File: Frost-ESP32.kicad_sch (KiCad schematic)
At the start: 28 parts, among them J1 Micro_SD_Card, J2 CAN, J3 USB_C_Receptacle, J4 Conn_01x10, SW1 SW_Push, U1 ESP32-C3-WROOM-02, U2 AP2112K-3.3, U3 TJA1051T-3

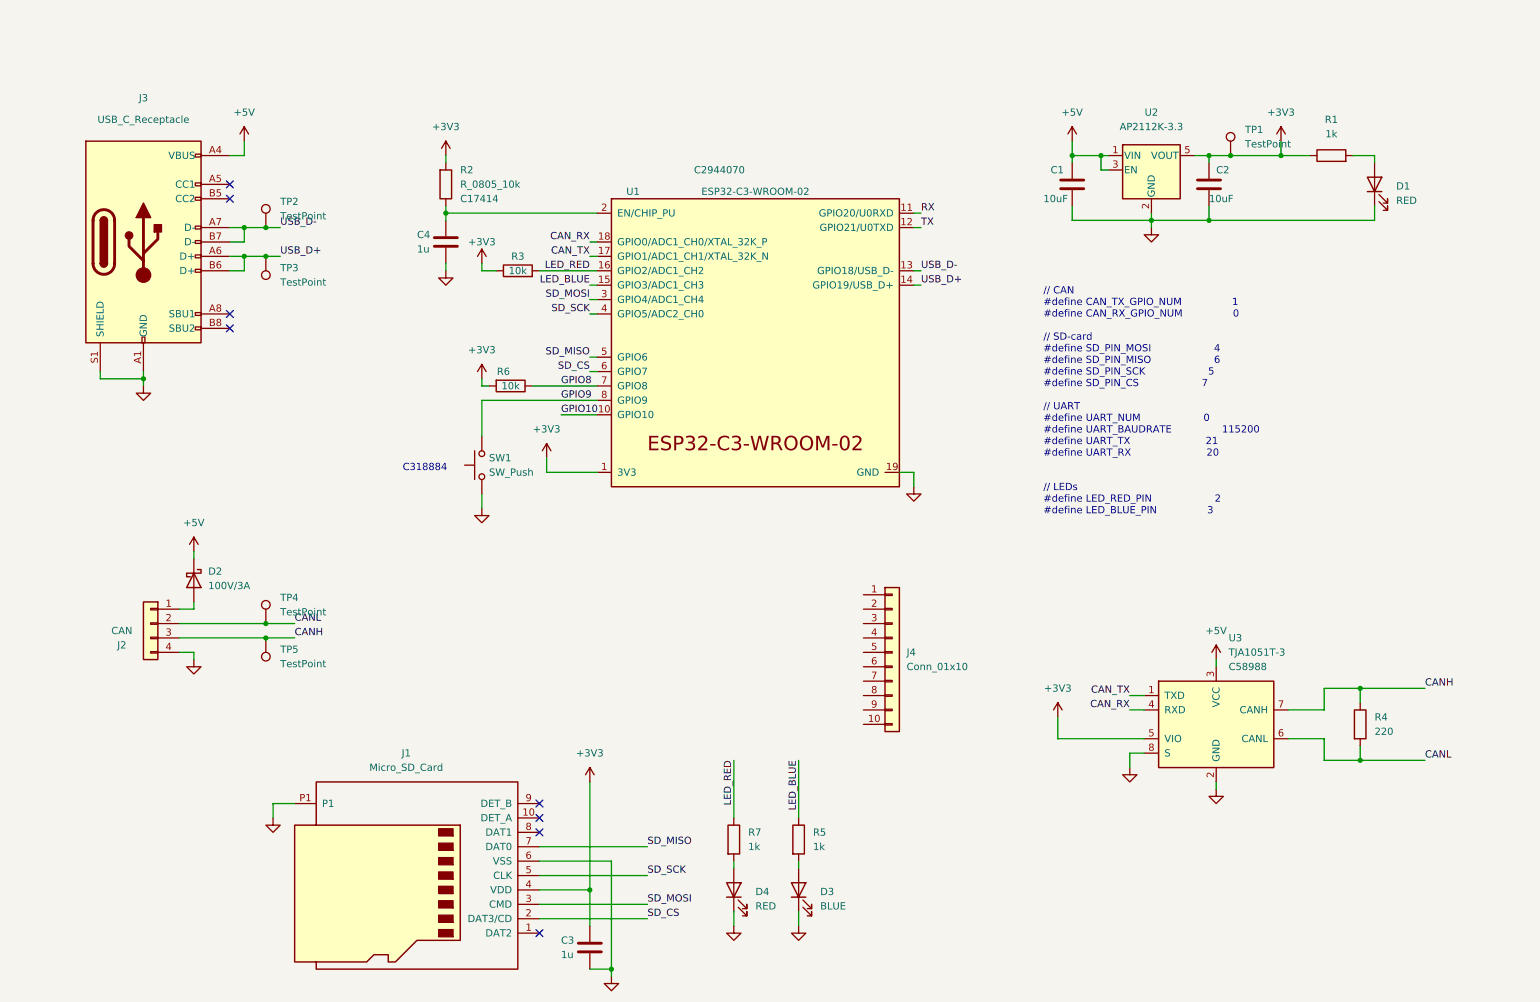
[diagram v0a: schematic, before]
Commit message: moved some symbols to fair library
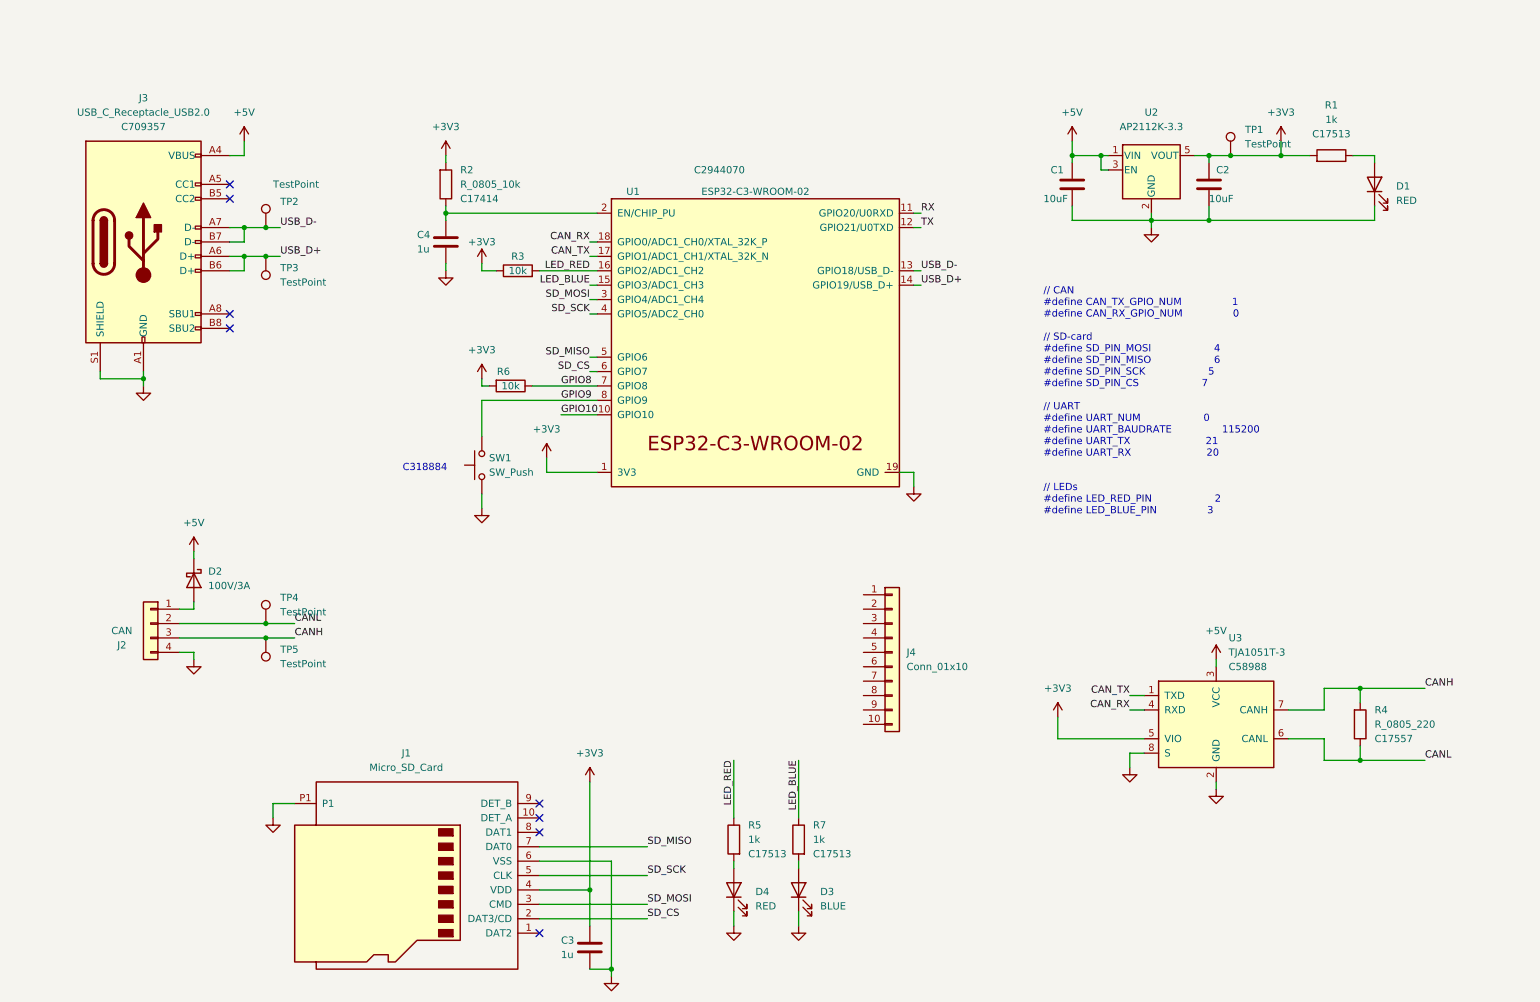
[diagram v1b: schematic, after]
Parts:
- removed J3: USB_C_Receptacle, Connector_USB:USB_C_Receptacle_XKB_U262-16XN-4BVC11, symbol Connector:USB_C_Receptacle_USB2.0
- removed R1, R5, R7: 1k, Resistor_SMD:R_0805_2012Metric, symbol Device:R
- removed R4: 220, Resistor_SMD:R_0805_2012Metric, symbol Device:R
- added J3: USB_C_Receptacle_USB2.0, Connector_USB:USB_C_Receptacle_XKB_U262-16XN-4BVC11, symbol Fair:USB_C_Receptacle_USB2.0
- added R1, R5, R7: 1k, Resistor_SMD:R_0805_2012Metric, symbol Fair:R_0805_1k
- added R4: R_0805_220, Resistor_SMD:R_0805_2012Metric, symbol Fair:R_0805_220
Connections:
- net +3V3: now also R1.1
- net +5V: now also J3.A4 (VBUS), J3.A9 (VBUS), J3.B4 (VBUS), J3.B9 (VBUS)
- net CANH: now also R4.1
- net CANL: now also R4.2
- net GND: now also J3.A1 (GND), J3.A12 (GND), J3.B1 (GND), J3.B12 (GND), J3.S1 (SHIELD)
- net LED_BLUE: now also R7.2
- net LED_RED: now also R5.2
- net USB_D+: now also J3.A6 (D+), J3.B6 (D+)
- net USB_D-: now also J3.A7 (D-), J3.B7 (D-)
- net at D1.2 (A): now also R1.2
- net at D3.2 (A): now also R7.1
- net at D4.2 (A): now also R5.1

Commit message: After ordering v0.1
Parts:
- removed C1, C2: 10uF, Capacitor_SMD:C_0805_2012Metric, symbol Device:C
- removed C3, C4: 1u, Capacitor_SMD:C_0805_2012Metric, symbol Device:C
- removed D1, D4: RED, LED_SMD:LED_0805_2012Metric, symbol Device:LED
- removed D3: BLUE, LED_SMD:LED_0603_1608Metric, symbol Device:LED
- removed J1: Micro_SD_Card, espressif:MOLEX_503398-1892, symbol Connector:Micro_SD_Card_Det
- removed J2: CAN, Connector_JST:JST_PH_B4B-PH-K_1x04_P2.00mm_Vertical, symbol Connector_Generic:Conn_01x04
- removed J3: USB_C_Receptacle_USB2.0, Connector_USB:USB_C_Receptacle_XKB_U262-16XN-4BVC11, symbol Fair:USB_C_Receptacle_USB2.0
- removed J4: Conn_01x10, Connector_PinHeader_2.54mm:PinHeader_1x10_P2.54mm_Vertical, symbol Connector_Generic:Conn_01x10
- removed R1, R5, R7: 1k, Resistor_SMD:R_0805_2012Metric, symbol Fair:R_0805_1k
- removed R2: R_0805_10k, Resistor_SMD:R_0805_2012Metric, symbol Fair:R_0805_10k
- removed R3, R6: 10k, Resistor_SMD:R_0805_2012Metric, symbol Device:R
- removed R4: R_0805_220, Resistor_SMD:R_0805_2012Metric, symbol Fair:R_0805_220
- removed SW1: SW_Push, Button_Switch_SMD:SW_Push_1P1T_XKB_TS-1187A, symbol Switch:SW_Push
- added C1, C2: 10uF/6.3V, Capacitor_SMD:C_0402_1005Metric, symbol Fair:C_0402_10uF/6.3V
- added C3: 1uF/25V, Capacitor_SMD:C_0402_1005Metric, symbol Fair:C_0402_1uF/25V
- added D1: Red, LED_SMD:LED_0603_1608Metric, symbol Fair:LED_0603_Red
- added D3: Blue, LED_SMD:LED_0603_1608Metric, symbol Fair:LED_BLUE_0603
- added D4: Emerald, LED_SMD:LED_0603_1608Metric, symbol Fair:LED_0603_Emerald
- added D5: 100V/3A, Diode_SMD:D_SOD-123F, symbol Device:D_Schottky
- added H1, H2: MountingHole, MountingHole:MountingHole_3.2mm_M3, symbol Mechanical:MountingHole
- added J1: Micro_SD_Card, Fair:MOLEX_503398-1892, symbol Fair:Micro_SD_Card_Det
- added J2: CAN, Connector_PinHeader_1.27mm:PinHeader_1x10_P1.27mm_Vertical, symbol Connector_Generic:Conn_01x10
- added J3: USB__B_Micro_Horizontal, Connector_USB:USB_Micro-B_Molex_47346-0001, symbol Fair:USB__B_Micro_Horizontal
- added R1, R5, R7: 1k, Resistor_SMD:R_0402_1005Metric, symbol Fair:R_0402_1k
- added R2, R3, R6: 10k, Resistor_SMD:R_0402_1005Metric, symbol Fair:R_0402_10k
- added R4: 220, Resistor_SMD:R_0402_1005Metric, symbol Fair:R_0402_220
- added S1: TL3340AF160QG, Fair:SW_TL3340AF160QG, symbol Fair:Switch_SMD_TL3340AF160QG
- added TP6, TP7: TestPoint, TestPoint:TestPoint_Pad_D1.0mm, symbol Connector:TestPoint
- U1: LCSC C2944070 -> C2934560
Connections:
- net +3V3: now also C2.1, J1.4 (VDD), R2.2, R3.1, R6.1, R7.1
- net +5V: now also C1.1, D5.1 (K), J2.5 (Pin_5)
- net CANH: now also J2.3 (Pin_3), R4.2
- net CANL: now also J2.2 (Pin_2), R4.1
- net GND: now also C1.2, C2.2, C3.2, D1.1 (K), D3.1 (K), D4.1 (K), J1.6 (VSS), J1.P1, J2.10 (Pin_10), J2.4 (Pin_4), J3.5 (GND), J3.6 (Shield), S1.1, S1.3
- net GPIO10: now also J2.9 (Pin_9)
- net GPIO8: now also J2.8 (Pin_8), R6.2
- net GPIO9: now also S1.2
- net RX: now also J2.6 (Pin_6), TP6.1
- net SD_CS: now also J1.2 (DAT3/CD)
- net SD_MISO: now also J1.7 (DAT0)
- net SD_MOSI: now also J1.3 (CMD)
- net SD_SCK: now also J1.5 (CLK)
- net TX: now also J2.7 (Pin_7), TP7.1
- net USB_D+: now also J3.3 (D+)
- net USB_D-: now also J3.2 (D-)
- net at U1.2 (EN/CHIP_PU): now also C3.1, R2.1
- net Vconn: now reaches D2.2 (A)
- net Vconn: now also J2.1 (Pin_1)
- net LED_BLUE renamed LED_Blue
- net LED_Blue: now also R5.2
- net LED_RED renamed LED_Green
- net LED_Green: now also R1.2, R3.2
- new net: D3.2 (A), R5.1
- new net: D1.2 (A), R7.2
- new net: D4.2 (A), R1.1
- new net Vbus: D5.2 (A), J3.1 (VBUS)
- no-connect marks 8 -> 5
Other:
- note added: "C318884 (too big)"
- note removed: "C318884"
- moved on the sheet: D2, TP2, TP3
